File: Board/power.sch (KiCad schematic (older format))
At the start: 20 parts, among them U1 TPS54531

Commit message: Routing done.
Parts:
- removed C10, C11: ???, symbol Device:C
- removed C5: 2200pF/50V, symbol Device:C
- removed C6: 22pF/50V, symbol Device:C
- removed U1: TPS54531, symbol power_custom:TPS54531
- added C10, C6: 47uF/25V, symbol Device:CP
- added C5: 33uF/10V, symbol Device:CP
- added D2: D_Schottky, symbol Device:D_Schottky
- added F1, F2: Polyfuse, symbol Device:Polyfuse
- added L2: 10uH, symbol Device:L
- added Q1, Q2: Q_PMOS_GDS, Package_TO_SOT_SMD:TO-263-2, symbol Device:Q_PMOS_GDS
- added R10: 1.15k, symbol Device:R
- added R7: 4.12k, symbol Device:R
- added R8: 10m, Resistor_SMD:R_1206_3216Metric_Pad1.42x1.75mm_HandSolder, symbol Device:R
- added R9: 10k, symbol Device:R
- added U1, U2: LM25085MY, Package_SO:MSOP-8-1EP_3x3mm_P0.65mm_EP1.68x1.88mm, symbol Regulator_Switching:LM25085MY
- C2: value 4.7uF/25V -> 1uF/25V
- C4: value 10nF/50V -> 750pF/15V
- C7: value 0.1uF/50V -> 1uF/25V
- C8: value 47uF/6.3V -> 1nF/50V
- C9: value 47uF/6.3V -> 12nF/15V
- D1: footprint Diode_SMD:D_SMC_Handsoldering -> (none); Farnell 1843671 -> 2773825; Ref B540C-13-F -> MBRD10200CT
- L1: value 4.7uH -> 8.2uH; Farnell 2077823 -> 2289089; Ref 74437368047 -> XAL6060-822MEC
- R1: value 665k -> 44.2k
- R2: value 130k -> 2.21k
- R3: value 37.4k -> 10m; footprint (none) -> Resistor_SMD:R_1206_3216Metric_Pad1.42x1.75mm_HandSolder; Farnell (none) -> 1099907; Ref (none) -> LRF1206-R01FW
- R4: value 51.1k -> 10k
- R5: value 10.2k -> 3.32k
- R6: value 1.96k -> 383k
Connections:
- net +5V: now also F1.1; no longer C8.1, C9.1, L1.1, R4.1
- net BATT+: now also C3.2, C7.1, C8.2, R2.1, R3.2, R6.1, C6.1, R7.1, R8.2, U1.8 (VIN), U2.8 (VIN); no longer C3.1
- net GND: now also R5.1, C10.2, C5.2, C6.2, D2.2 (A), R10.1, U1.4 (GND), U1.9 (EP), U2.4 (GND), U2.9 (EP); no longer C2.2, C3.2, C4.1, C8.2, C9.2, R2.2, R3.2, R6.2
- net at C7.2: now also U2.7 (VCC)
- net at R1.2: now also U1.2 (RT); no longer R2.1
- net at C4.2: now also R4.1, R5.2, U1.3 (FB)
- net at R3.1: now also Q1.3 (S), U1.5 (ISEN)
- net at R4.2: now also C4.1, L1.2, C5.1, F1.2; no longer R5.1
- new net: C3.1, R2.2, U1.1 (ADJ)
- new net: Q1.1 (G), U1.6 (PGATE)
- new net: C2.2, U1.7 (VCC)
- new net: D1.1 (K), L1.1, Q1.2 (D)
- new net: C8.1, R7.2, U2.1 (ADJ)
- new net: R6.2, U2.2 (RT)
- new net: C9.2, R10.2, R9.1, U2.3 (FB)
- new net: Q2.3 (S), R8.1, U2.5 (ISEN)
- new net: Q2.1 (G), U2.6 (PGATE)
- new net: D2.1 (K), L2.1, Q2.2 (D)
- new net: C10.1, C9.1, F2.2, L2.2, R9.2
- new net +12V: F2.1
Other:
- note added: "12V@10A"
- note added: "5V@5A"
- moved on the sheet: C1

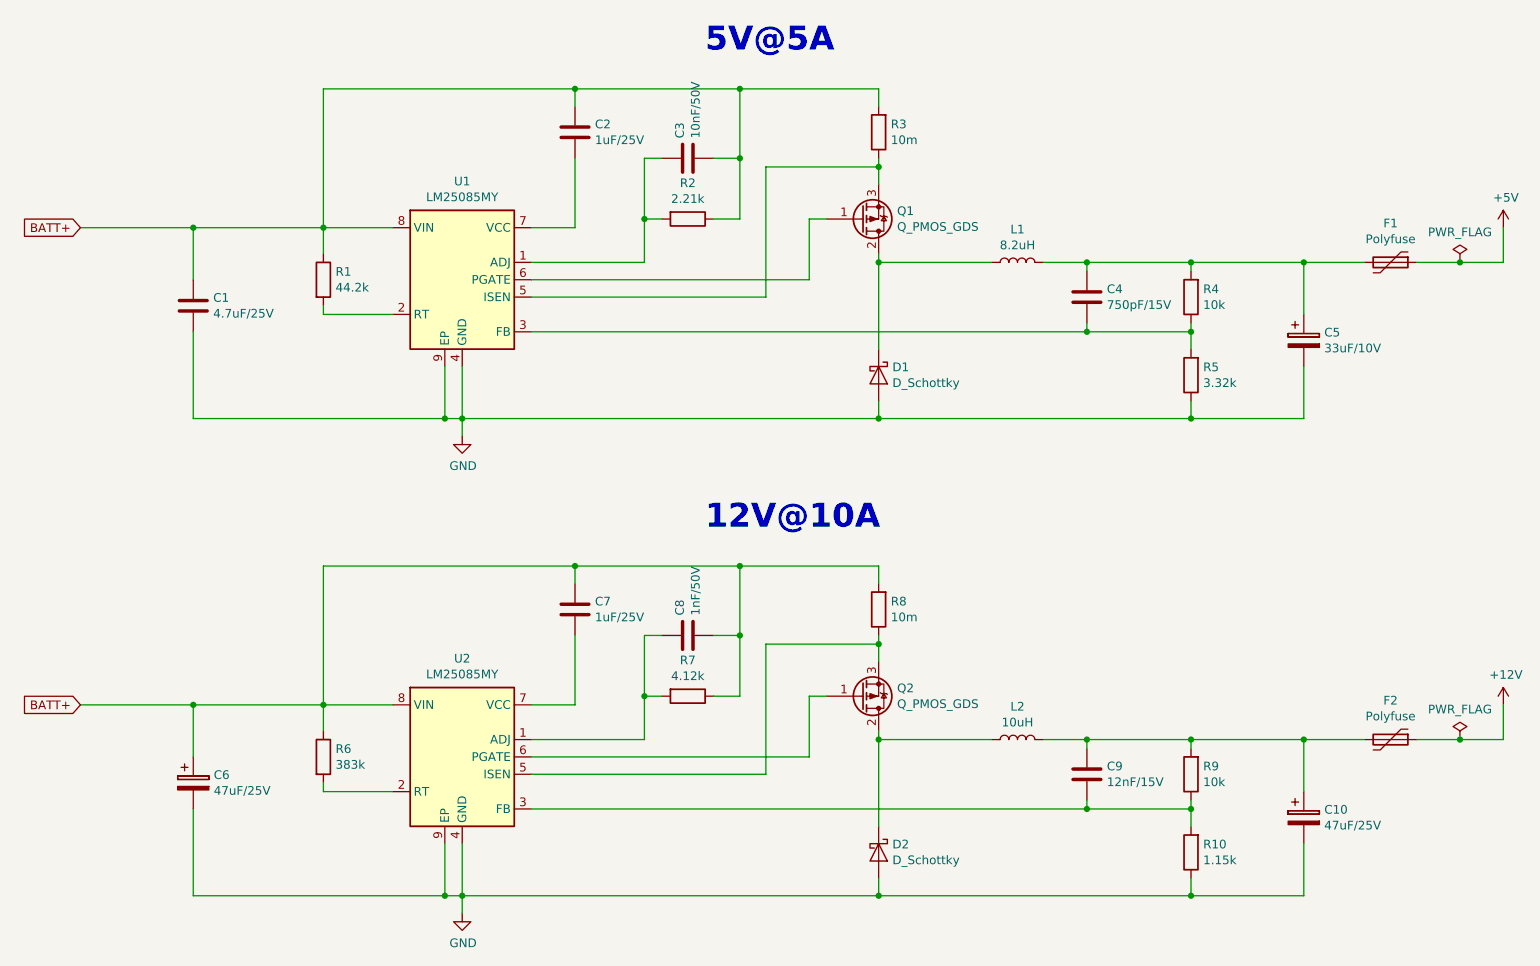
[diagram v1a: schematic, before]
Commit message: Routing done, waiting for mechanical integration.
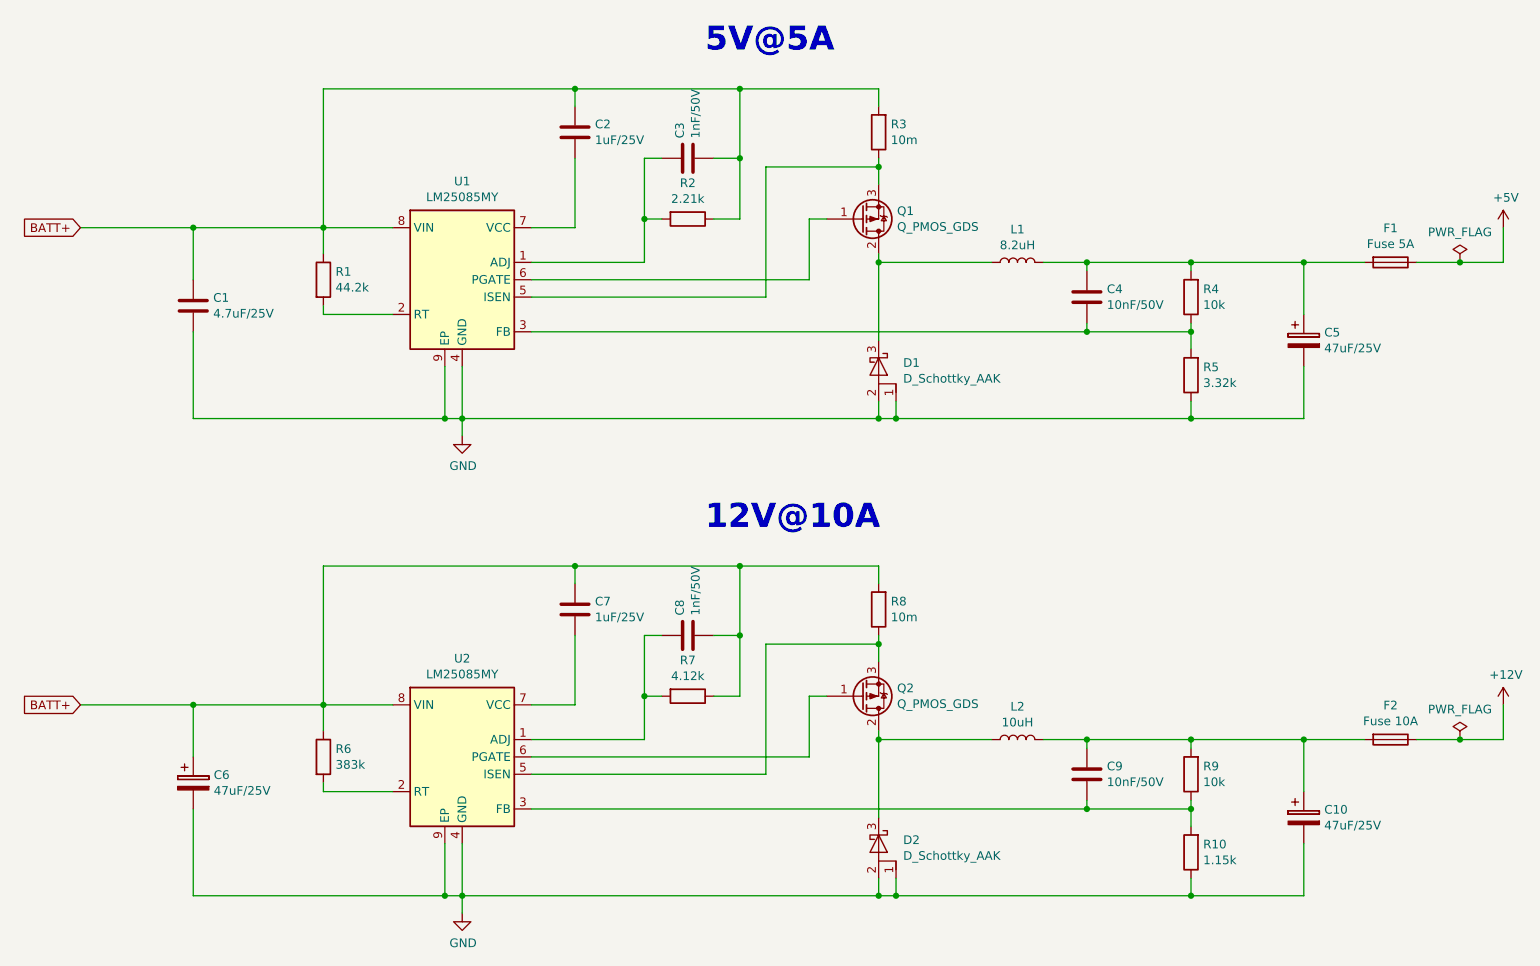
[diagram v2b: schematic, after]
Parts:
- removed D1, D2: D_Schottky, symbol Device:D_Schottky
- removed F1, F2: Polyfuse, symbol Device:Polyfuse
- added D1, D2: D_Schottky_AAK, Package_TO_SOT_SMD:TO-252-2, symbol Device:D_Schottky_AAK
- added F1: Fuse 5A, Fuses_custom:Fuse_holder_Littelfuse_154, symbol Device:Fuse
- added F2: Fuse 10A, Fuses_custom:Fuse_holder_Littelfuse_154, symbol Device:Fuse
- C1: footprint (none) -> Capacitor_SMD:C_0805_2012Metric_Pad1.15x1.40mm_HandSolder
- C10, C6: footprint (none) -> Capacitors:25SVPF47M
- C2, C7, C8: footprint (none) -> Capacitor_SMD:C_0603_1608Metric_Pad1.05x0.95mm_HandSolder
- C3: value 10nF/50V -> 1nF/50V; footprint (none) -> Capacitor_SMD:C_0603_1608Metric_Pad1.05x0.95mm_HandSolder
- C4: value 750pF/15V -> 10nF/50V; footprint (none) -> Capacitor_SMD:C_0603_1608Metric_Pad1.05x0.95mm_HandSolder
- C5: value 33uF/10V -> 47uF/25V; footprint (none) -> Capacitors:25SVPF47M; Farnell (none) -> 2354803; Ref (none) -> 25SVPF47M
- C9: value 12nF/15V -> 10nF/50V; footprint (none) -> Capacitor_SMD:C_0603_1608Metric_Pad1.05x0.95mm_HandSolder
- L1: footprint (none) -> Inductors:Coilcraft_XAL6060-822MEC
- L2: footprint (none) -> Inductors:Coilcraft_SER2915L-103KL
- R1, R10, R2, R4, R5, R6, R7, R9: footprint (none) -> Resistor_SMD:R_0603_1608Metric_Pad1.05x0.95mm_HandSolder
- U1, U2: footprint Package_SO:MSOP-8-1EP_3x3mm_P0.65mm_EP1.68x1.88mm -> TexasInstruments:LM25085MY_Handsolder
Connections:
- net +12V: now also F2.1
- net +5V: now also F1.1
- net GND: now also D1.1 (A), D1.2 (A), D2.1 (A), D2.2 (A)
- net at L1.1, Q1.2 (D): now also D1.3 (K)
- net at C4.1, C5.1, L1.2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: now also F1.2
- net at L2.1, Q2.2 (D): now also D2.3 (K)
- net at C10.1, C9.1, L2.2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: now also F2.2

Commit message: REPLACE PREVIOUS COMMIT.
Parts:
- added C11: 47uF/25V, Capacitors:25SVPF47M, symbol Device:CP
- R3: value 10m -> 10m/0.5W; Farnell 1099907 -> 2805340; Ref LRF1206-R01FW -> RLP73V2BR010FTDF
- R8: value 10m -> 10m/1.5W; footprint Resistor_SMD:R_1206_3216Metric_Pad1.42x1.75mm_HandSolder -> Resistor_SMD:R_2010_5025Metric_Pad1.52x2.65mm_HandSolder; Farnell 1099907 -> 2332264; Ref LRF1206-R01FW -> TLR2H15DR010FTDG
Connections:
- net BATT+: now also C11.1
- net GND: now also C11.2
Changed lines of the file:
@@
 P 6800 1200
 F 0 "R3" H 6730 1154 50  0000 R CNN
-F 1 "10m" H 6730 1245 50  0000 R CNN
+F 1 "10m/0.5W" H 6730 1245 50  0000 R CNN
 F 2 "Resistor_SMD:R_1206_3216Metric_Pad1.42x1.75mm_HandSolder" V 6730 1200 50  0001 C CNN
 F 3 "~" H 6800 1200 50  0001 C CNN
-F 4 "1099907" H 6800 1200 50  0001 C CNN "Farnell"
-F 5 "LRF1206-R01FW" H 6800 1200 50  0001 C CNN "Ref"
+F 4 "2805340" H 6800 1200 50  0001 C CNN "Farnell"
+F 5 "RLP73V2BR010FTDF" H 6800 1200 50  0001 C CNN "Ref"
 	1    6800 1200
 	-1   0    0    1
@@
 $EndComp
 Wire Wire Line
-	2200 4500 2850 4500
+	2200 4500 2550 4500
 Wire Wire Line
 	3600 4650 3600 4500
@@
 P 6800 3950
 F 0 "R8" H 6730 3904 50  0000 R CNN
-F 1 "10m" H 6730 3995 50  0000 R CNN
-F 2 "Resistor_SMD:R_1206_3216Metric_Pad1.42x1.75mm_HandSolder" V 6730 3950 50  0001 C CNN
+F 1 "10m/1.5W" H 6730 3995 50  0000 R CNN
+F 2 "Resistor_SMD:R_2010_5025Metric_Pad1.52x2.65mm_HandSolder" V 6730 3950 50  0001 C CNN
 F 3 "~" H 6800 3950 50  0001 C CNN
-F 4 "1099907" H 6800 3950 50  0001 C CNN "Farnell"
-F 5 "LRF1206-R01FW" H 6800 3950 50  0001 C CNN "Ref"
+F 4 "2332264" H 6800 3950 50  0001 C CNN "Farnell"
+F 5 "TLR2H15DR010FTDG" H 6800 3950 50  0001 C CNN "Ref"
 	1    6800 3950
 	-1   0    0    1
@@
 	1    0    0    -1
 $EndComp
+$Comp
+L Device:CP C11
+U 1 1 5C687BF1
+P 2550 4950
+F 0 "C11" H 2250 5000 50  0000 L CNN
+F 1 "47uF/25V" H 2050 4900 50  0000 L CNN
+F 2 "Capacitors:25SVPF47M" H 2588 4800 50  0001 C CNN
+F 3 "~" H 2550 4950 50  0001 C CNN
+F 4 "2354803" H 2550 4950 50  0001 C CNN "Farnell"
+F 5 "25SVPF47M" H 2550 4950 50  0001 C CNN "Ref"
+	1    2550 4950
+	1    0    0    -1
+$EndComp
+Wire Wire Line
+	2550 4800 2550 4500
+Connection ~ 2550 4500
+Wire Wire Line
+	2550 4500 2850 4500
+Wire Wire Line
+	2550 5100 2550 5600
+Wire Wire Line
+	2550 5600 2850 5600
+Connection ~ 2850 5600
 $EndSCHEMATC

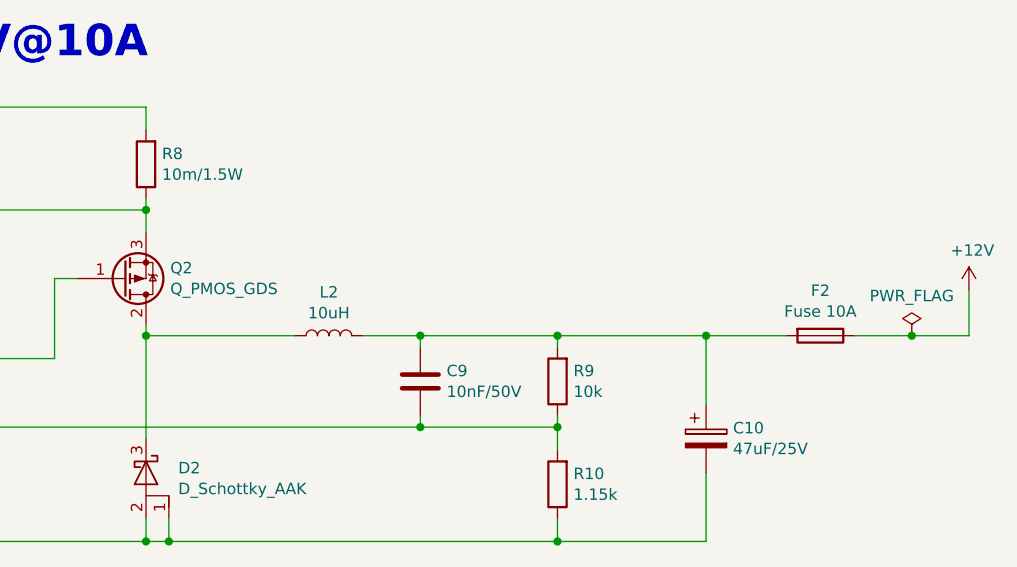
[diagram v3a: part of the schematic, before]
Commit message: Added one fuse and changed 10mOhm res to withstand 12A+
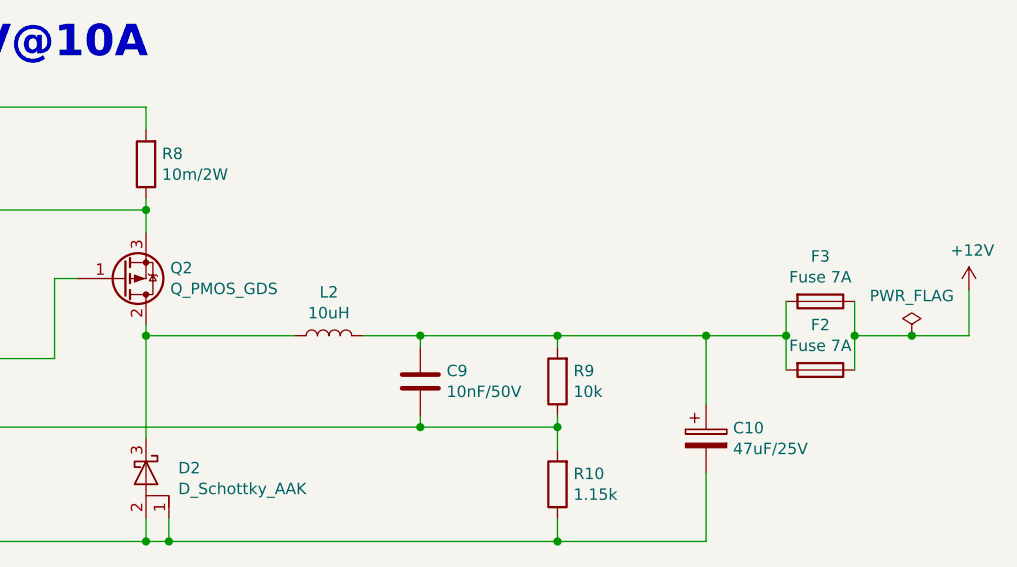
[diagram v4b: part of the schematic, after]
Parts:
- added F3: Fuse 7A, Fuses_custom:Fuse_holder_Littelfuse_154, symbol Device:Fuse
- F2: value Fuse 10A -> Fuse 7A; Farnell 1817192 -> 1817189; Ref 0154010.DR -> 0154007.DR
- R8: value 10m/1.5W -> 10m/2W; footprint Resistor_SMD:R_2010_5025Metric_Pad1.52x2.65mm_HandSolder -> Resistor_SMD:R_2512_6332Metric_Pad1.52x3.35mm_HandSolder; Farnell 2332264 -> 2805343; Ref TLR2H15DR010FTDG -> RLP73V3AR010FTDF
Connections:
- net +12V: now also F3.1
- net at C10.1, C9.1, F2.2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: now also F3.2
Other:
- moved on the sheet: F2
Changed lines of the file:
@@
 Connection ~ 8600 5600
-Wire Wire Line
-	9250 5000 9250 4700
 Wire Wire Line
 	9250 4700 8600 4700
 Connection ~ 8600 4700
-Wire Wire Line
-	9250 4700 9600 4700
-Connection ~ 9250 4700
 Wire Wire Line
 	9900 4700 10150 4700
@@
 P 6800 3950
 F 0 "R8" H 6730 3904 50  0000 R CNN
-F 1 "10m/1.5W" H 6730 3995 50  0000 R CNN
-F 2 "Resistor_SMD:R_2010_5025Metric_Pad1.52x2.65mm_HandSolder" V 6730 3950 50  0001 C CNN
+F 1 "10m/2W" H 6730 3995 50  0000 R CNN
+F 2 "Resistor_SMD:R_2512_6332Metric_Pad1.52x3.35mm_HandSolder" V 6730 3950 50  0001 C CNN
 F 3 "~" H 6800 3950 50  0001 C CNN
-F 4 "2332264" H 6800 3950 50  0001 C CNN "Farnell"
-F 5 "TLR2H15DR010FTDG" H 6800 3950 50  0001 C CNN "Ref"
+F 4 "2805343" H 6800 3950 50  0001 C CNN "Farnell"
+F 5 "RLP73V3AR010FTDF" H 6800 3950 50  0001 C CNN "Ref"
 	1    6800 3950
 	-1   0    0    1
@@
 L Device:Fuse F2
 U 1 1 5C4CC3EC
-P 9750 4700
-F 0 "F2" V 9553 4700 50  0000 C CNN
-F 1 "Fuse 10A" V 9644 4700 50  0000 C CNN
-F 2 "Fuses_custom:Fuse_holder_Littelfuse_154" V 9680 4700 50  0001 C CNN
-F 3 "~" H 9750 4700 50  0001 C CNN
-F 4 "1817192" H 9750 4700 50  0001 C CNN "Farnell"
-F 5 "0154010.DR" H 9750 4700 50  0001 C CNN "Ref"
-	1    9750 4700
+P 9750 4850
+F 0 "F2" V 9553 4850 50  0000 C CNN
+F 1 "Fuse 7A" V 9644 4850 50  0000 C CNN
+F 2 "Fuses_custom:Fuse_holder_Littelfuse_154" V 9680 4850 50  0001 C CNN
+F 3 "~" H 9750 4850 50  0001 C CNN
+F 4 "1817189" H 9750 4850 50  0001 C CNN "Farnell"
+F 5 "0154007.DR" H 9750 4850 50  0001 C CNN "Ref"
+	1    9750 4850
 	0    1    1    0
 $EndComp
@@
 	2550 5600 2850 5600
 Connection ~ 2850 5600
+$Comp
+L Device:Fuse F3
+U 1 1 5CA3B268
+P 9750 4550
+F 0 "F3" V 9553 4550 50  0000 C CNN
+F 1 "Fuse 7A" V 9644 4550 50  0000 C CNN
+F 2 "Fuses_custom:Fuse_holder_Littelfuse_154" V 9680 4550 50  0001 C CNN
+F 3 "~" H 9750 4550 50  0001 C CNN
+F 4 "1817189" H 9750 4550 50  0001 C CNN "Farnell"
+F 5 "0154007.DR" H 9750 4550 50  0001 C CNN "Ref"
+	1    9750 4550
+	0    1    1    0
+$EndComp
+Wire Wire Line
+	9250 4700 9250 5000
+Wire Wire Line
+	9250 4700 9600 4700
+Wire Wire Line
+	9600 4700 9600 4550
+Connection ~ 9250 4700
+Wire Wire Line
+	9600 4700 9600 4850
+Connection ~ 9600 4700
+Wire Wire Line
+	9900 4850 9900 4700
+Wire Wire Line
+	9900 4550 9900 4700
+Connection ~ 9900 4700
 $EndSCHEMATC

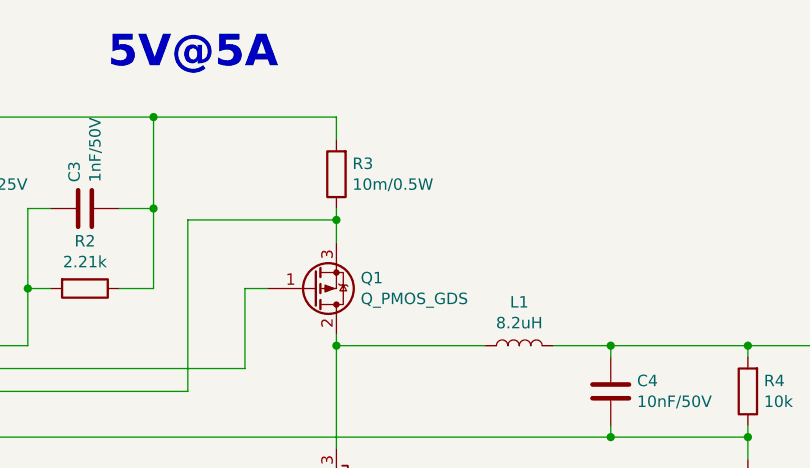
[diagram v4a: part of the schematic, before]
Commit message: Used to 2W res instead of one 0.5W + one 2W
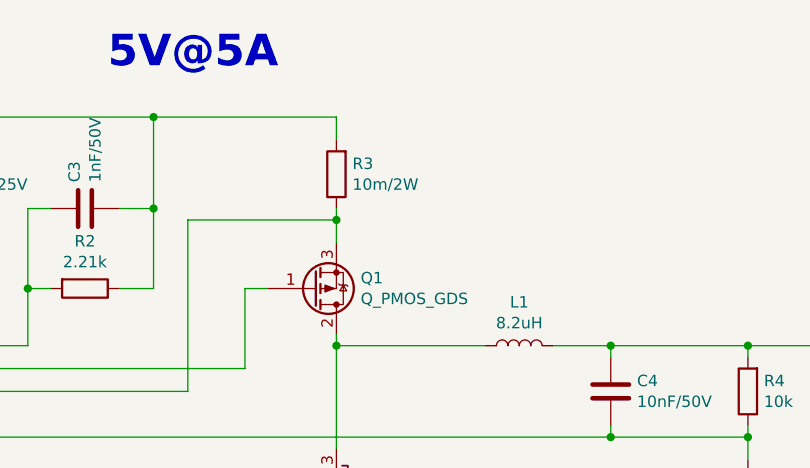
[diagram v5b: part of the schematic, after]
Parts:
- R3: value 10m/0.5W -> 10m/2W; footprint Resistor_SMD:R_1206_3216Metric_Pad1.42x1.75mm_HandSolder -> Resistor_SMD:R_2512_6332Metric_Pad1.52x3.35mm_HandSolder; Farnell 2805340 -> 2332326; Ref RLP73V2BR010FTDF -> TLR3A20ER010FTDG
- R8: Farnell 2805343 -> 2332326; Ref RLP73V3AR010FTDF -> TLR3A20ER010FTDG
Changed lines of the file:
@@
 	1    0    0    1
-$EndComp
-$Comp
-L Device:R R3
-U 1 1 5C49C460
-P 6800 1200
-F 0 "R3" H 6730 1154 50  0000 R CNN
-F 1 "10m/0.5W" H 6730 1245 50  0000 R CNN
-F 2 "Resistor_SMD:R_1206_3216Metric_Pad1.42x1.75mm_HandSolder" V 6730 1200 50  0001 C CNN
-F 3 "~" H 6800 1200 50  0001 C CNN
-F 4 "2805340" H 6800 1200 50  0001 C CNN "Farnell"
-F 5 "RLP73V2BR010FTDF" H 6800 1200 50  0001 C CNN "Ref"
-	1    6800 1200
-	-1   0    0    1
 $EndComp
 Wire Wire Line
@@
 $EndComp
 $Comp
-L Device:R R8
-U 1 1 5C4AF5DB
-P 6800 3950
-F 0 "R8" H 6730 3904 50  0000 R CNN
-F 1 "10m/2W" H 6730 3995 50  0000 R CNN
-F 2 "Resistor_SMD:R_2512_6332Metric_Pad1.52x3.35mm_HandSolder" V 6730 3950 50  0001 C CNN
-F 3 "~" H 6800 3950 50  0001 C CNN
-F 4 "2805343" H 6800 3950 50  0001 C CNN "Farnell"
-F 5 "RLP73V3AR010FTDF" H 6800 3950 50  0001 C CNN "Ref"
-	1    6800 3950
-	-1   0    0    1
-$EndComp
-$Comp
 L Device:CP C6
 U 1 1 5C4AFD52
@@
 	9900 4550 9900 4700
 Connection ~ 9900 4700
+$Comp
+L Device:R R3
+U 1 1 5CCDF1DC
+P 6800 1200
+F 0 "R3" H 6730 1154 50  0000 R CNN
+F 1 "10m/2W" H 6730 1245 50  0000 R CNN
+F 2 "Resistor_SMD:R_2512_6332Metric_Pad1.52x3.35mm_HandSolder" V 6730 1200 50  0001 C CNN
+F 3 "~" H 6800 1200 50  0001 C CNN
+F 4 "2332326" H 6800 1200 50  0001 C CNN "Farnell"
+F 5 "TLR3A20ER010FTDG" H 6800 1200 50  0001 C CNN "Ref"
+	1    6800 1200
+	-1   0    0    1
+$EndComp
+$Comp
+L Device:R R8
+U 1 1 5C4AF5DB
+P 6800 3950
+F 0 "R8" H 6730 3904 50  0000 R CNN
+F 1 "10m/2W" H 6730 3995 50  0000 R CNN
+F 2 "Resistor_SMD:R_2512_6332Metric_Pad1.52x3.35mm_HandSolder" V 6730 3950 50  0001 C CNN
+F 3 "~" H 6800 3950 50  0001 C CNN
+F 4 "2332326" H 6800 3950 50  0001 C CNN "Farnell"
+F 5 "TLR3A20ER010FTDG" H 6800 3950 50  0001 C CNN "Ref"
+	1    6800 3950
+	-1   0    0    1
+$EndComp
 $EndSCHEMATC
